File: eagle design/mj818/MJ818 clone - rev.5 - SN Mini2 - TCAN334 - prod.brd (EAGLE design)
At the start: 36 x 36 mm, 39 parts, among them IC202 LDK320AM33R, IC402 STM32F042G6U6, IC501 TCAN334, IC606 MAX16820, IC607 SQA470EEJ-T1_GE3, IC701 MAX16839

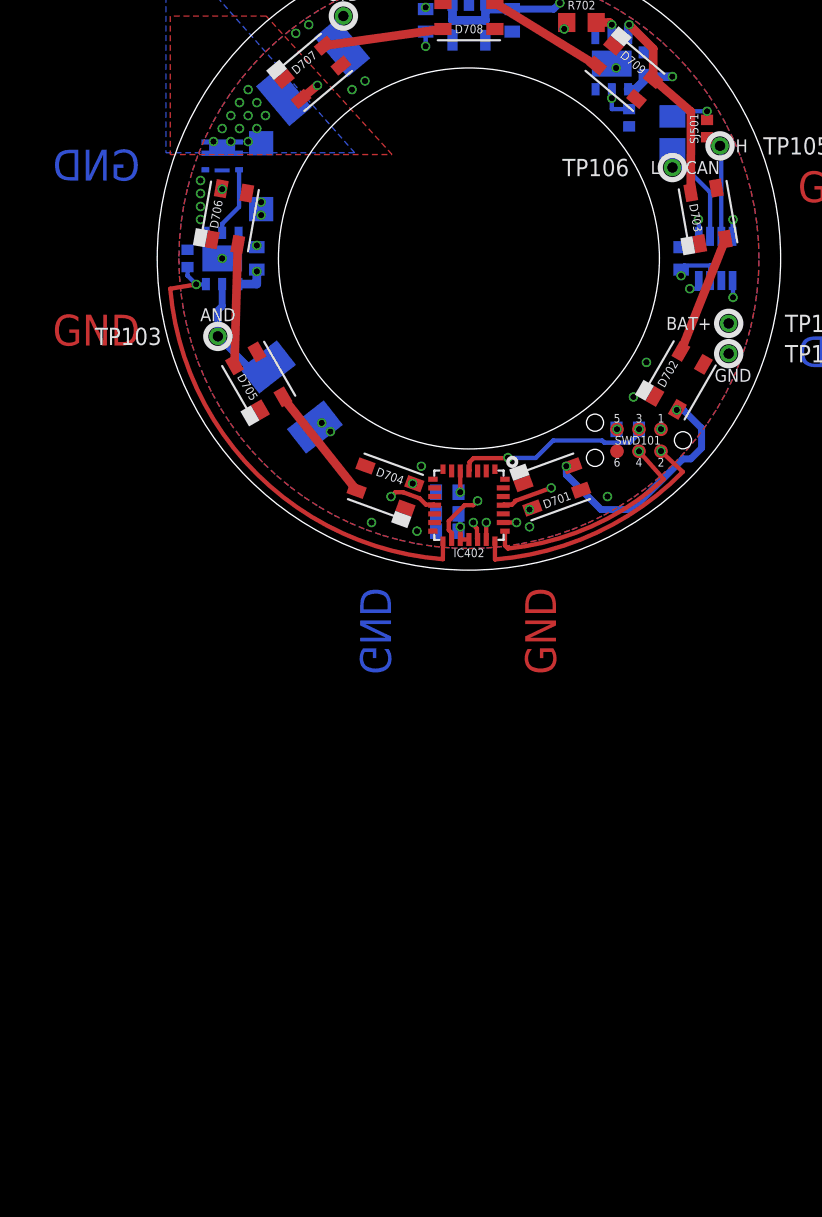
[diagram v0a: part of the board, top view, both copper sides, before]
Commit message: - renamed prod brd & sch files to reflect development for the SuperNova Mini2 housing - added docu & info to reflect housing design
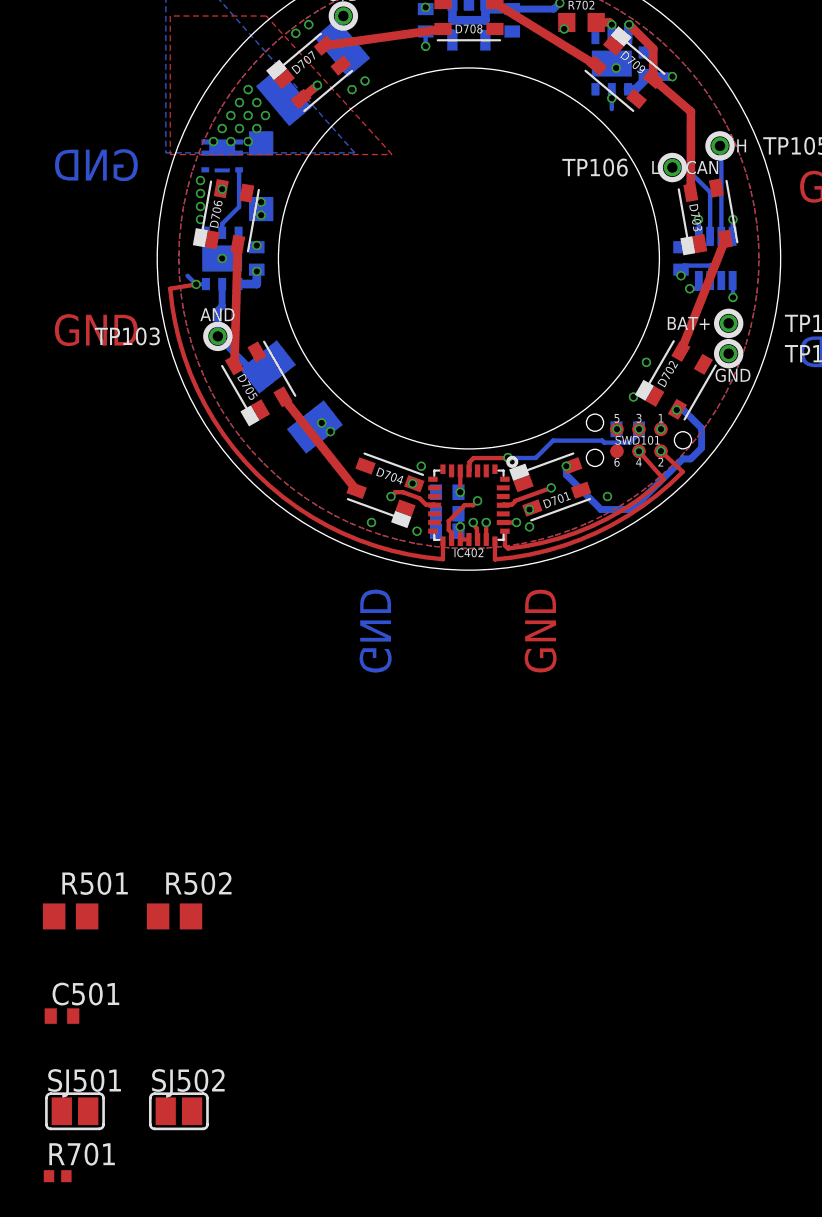
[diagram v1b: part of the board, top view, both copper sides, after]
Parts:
- removed R101, R102: 10k, rcl:R0402
- removed R505: 120, rcl:R0805
- added C501: 47nF / 10V, rcl:C0402
- added R501, R502: 60, rcl:R0805
- added R701: 10k, rcl:R0402
- added SJ502: CAN L term., jumper:SJ
- SJ501: value CAN termination -> CAN H term.; device rcl:R0402 -> jumper:SJ
- moved SJ501 67.5 mm to (-22.8, -49.2), turned to 0 degrees
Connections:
- removed net CAN_INFRA:CAN_JMPR: R505.2, SJ501.1
- new net CAN_INFRA:H: R502.2, SJ501.2
- new net CAN_INFRA:L: R501.1, SJ502.2
- new net CAN_INFRA:SPLIT: C501.1, R501.2, R502.1
- net CAN_H: now also SJ501.1; no longer SJ501.2
- net CAN_L: now also SJ502.1; no longer R505.1
- net DIM_BRAKE: no longer R101.2
- net DIM_REAR: now also R701.2; no longer R102.2
- net GND: now also C501.2, R701.1; no longer R101.1, R102.1
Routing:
- net CAN_INFRA:CAN_JMPR: track 2.62 -> 0.00 mm, vias 1 -> 0
- net CAN_L: track 6.37 -> 5.32 mm
- net DIM_REAR: track 33.0 -> 32.0 mm
- net CAN_H: track 6.21 -> 5.51 mm
- net DIM_BRAKE: track 26.5 -> 26.0 mm
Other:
- board text added: "SuperNova Mini2 housing"

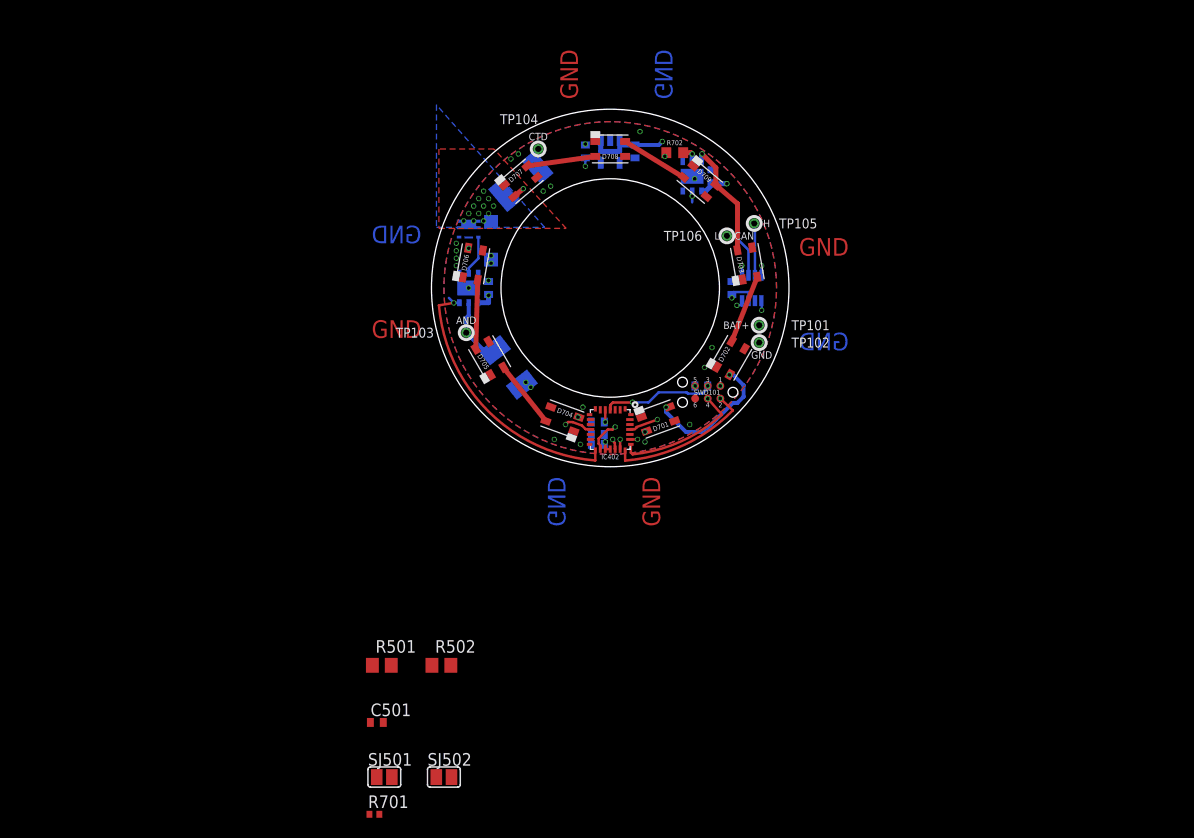
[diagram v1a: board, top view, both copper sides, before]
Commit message: - adjusted PCB outline to match new housing
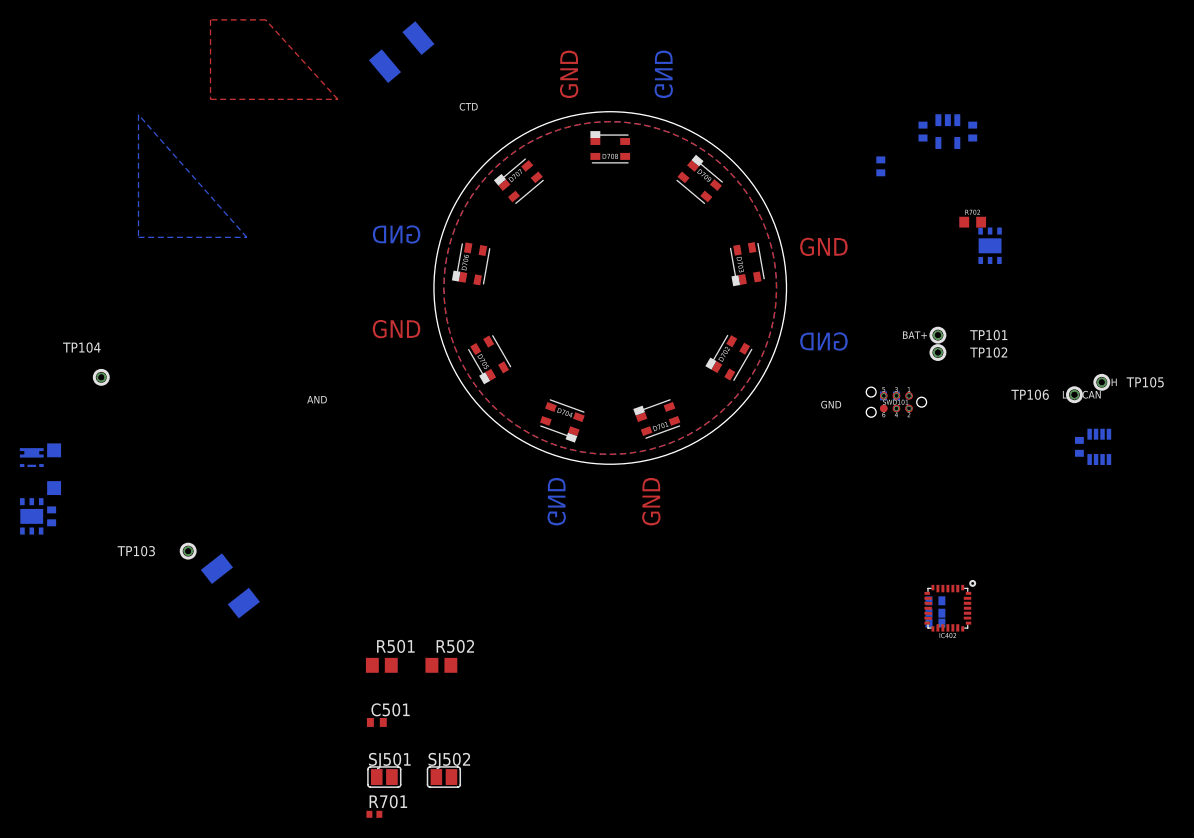
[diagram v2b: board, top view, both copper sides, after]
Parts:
- moved C606 49.6 mm to (-56.2, -23.0)
- moved D601 49.6 mm to (-56.0, -18.2)
- moved IC606 49.6 mm to (-58.2, -23.0)
- moved IC607 49.6 mm to (-58.2, -17.0)
- moved TP104 49.6 mm to (-51.2, -9.00)
- moved C505 38.5 mm to (47.2, -16.0)
- moved IC501 38.5 mm to (49.2, -16.0)
- moved TP105 38.5 mm to (49.5, -9.50)
- moved TP106 38.5 mm to (46.8, -10.8)
- moved C401 38.5 mm to (32.8, -33.8)
- moved C404 38.5 mm to (32.8, -31.5)
- moved C405 38.5 mm to (32.8, -32.8)
- moved IC402 38.5 mm to (34.0, -32.2)
- moved R608 35.6 mm to (-38.2, -30.0)
- moved TP103 35.6 mm to (-42.5, -26.5)
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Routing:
- net BAT+: track 96.5 -> 0.00 mm, vias 10 -> 0
- net REAR_LED_DRIVER:SINK: track 43.1 -> 0.00 mm, vias 2 -> 0
- net !STBY!: track 37.8 -> 0.00 mm, vias 2 -> 0
- net DIM_REAR: track 32.0 -> 0.00 mm, vias 3 -> 0
- net CAN_RX: track 28.7 -> 0.00 mm, vias 2 -> 0
- net CAN_TX: track 28.0 -> 0.00 mm, vias 2 -> 0
- net !SHDN!: track 26.4 -> 0.00 mm, vias 2 -> 0
- net DIM_BRAKE: track 26.0 -> 0.00 mm, vias 1 -> 0
- net SYS_SWDIO: track 14.8 -> 0.00 mm
- net REAR_LED_DRIVER:D1,D2: track 14.1 -> 0.00 mm, vias 2 -> 0
- net SYS_SWCLK: track 13.1 -> 0.00 mm
- net SYS_NRST: track 11.4 -> 0.00 mm, vias 2 -> 1
- net 3V3: track 9.60 -> 0.00 mm, vias 5 -> 1
- net REAR_LED_DRIVER:D2,D3: track 6.97 -> 0.00 mm
- net REAR_LED_DRIVER:D5,D6: track 6.97 -> 0.00 mm
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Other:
- board size 36 x 36 mm -> 35.5 x 35.5 mm

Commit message: - rough routing complete - corrected STM32 pin assignment of prod to match POC - ERC & DRC check out
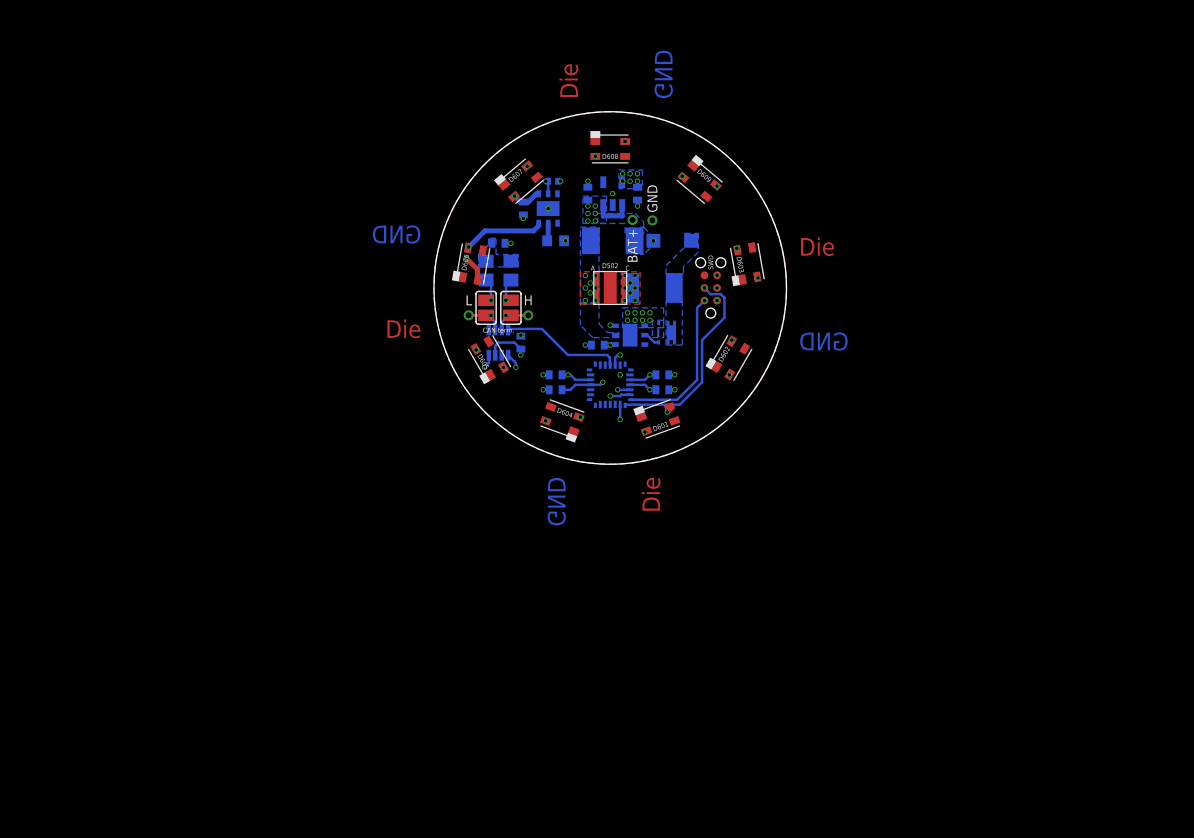
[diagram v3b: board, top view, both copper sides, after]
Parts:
- removed C404: 1u, rcl:C0402
- removed C407: 0.1u, rcl:C0402
- removed C501: 47nF / 10V, rcl:C0402
- removed C505: 0.1μF, rcl:C0402
- removed C606: 1μF / 10V, rcl:C0402
- removed C701: 1μF, rcl:C0402
- removed D701: CLM2D-RCC-CZ0B0BB3, 1374-CLM2D-RCC-ACC-1064252 - Red SMD LED:SMD
- removed IC402: STM32F042G6U6, STM32F042G6:UFQFPN-28
- removed IC501: TCAN334, TCAN33x - 3.3V CAN Transciever:SOT23-8
- removed IC606: MAX16820, MAX16820 LED Driver, constant current:TDFN-6-EP
- removed IC607: SQA470EEJ-T1_GE3, SIA456DJ-T1-GE3 N-Fet:SC-70-6
- removed IC701: MAX16839, MAX16839 LED Driver, constant current:TDFN-6-EP
- removed L601: SDE0604A-270M - 27uH, DE0604A-778075 - Inductor:SMT
- removed R501, R502: 60, rcl:R0805
- removed R608: WSLT2010R2200FEB18 / 0.22Ohm 1W, rcl:R2010
- removed R701: 10k, rcl:R0402
- removed R702: 10R/0.5W, rcl:R0603
- removed SJ501: CAN H term., jumper:SJ
- removed SJ502: CAN L term., jumper:SJ
- removed SWD101: TC2030-NL, tag-connect:TC2030-NL
- removed TP103: LED anode, signal testpoint:TH
- removed TP104: LED cathode, signal testpoint:TH
- added C301, C305, C307: 0.1uF / 10V, rcl:C0402
- added C304: 1uF / 10V, rcl:C0402
- added C506: 1μF / 10V, rcl:C0402
- added C601: 1μF, rcl:C0402
- added D501: PMEG2010ER,115, diode:SOD123
- added D502: Cree XPERED-L1-R250-00401, XLampXPE-221789:SMD
- added IC302: STM32F042G6U6, STM32F042G6:UFQFPN-28
- added IC401: TCAN334, TCAN33x - 3.3V CAN Transciever:SOT23-8
- added IC506: MAX16820, MAX16820 LED Driver, constant current:TDFN-6-EP
- added IC507: SQA470EEJ-T1_GE3, SIA456DJ-T1-GE3 N-Fet:SC-70-6
- added IC601: MAX16839, MAX16839 LED Driver, constant current:TDFN-6-EP
- added L501: SDE0604A-270M - 27uH, DE0604A-778075 - Inductor:SMT
- added R401, R402: 60, rcl:R0805
- added R508: WSLT2010R2200FEB18 / 0.22Ohm 1W, rcl:R2010
- added R601: 10k, rcl:R0402
- added R602: 10R/0.5W, rcl:R0603
- added SJ401: CAN H term., jumper:SJ
- added SJ402: CAN L term., jumper:SJ
- added SWD1: TC2030-NL, tag-connect:TC2030-NL
- C207: value 1μF -> 1uF / 10V
- C401: value 0.1u -> 47nF / 10V
- C405: value 0.1u -> 0.1uF / 10V
- D601: value PMEG2010ER,115 -> CLM2D-RCC-CZ0B0BB3; device diode:SOD123 -> 1374-CLM2D-RCC-ACC-1064252 - Red SMD LED:SMD
- TP101, TP102, TP105, TP106: device signal testpoint:TH -> signal testpoint:TH-0.6
- moved TP106 61.5 mm to (-14.2, -2.75), flipped to the bottom, turned to 180 degrees
- moved D601 61.0 mm to (4.82, -13.2), flipped to the top, turned to 20 degrees
- moved C401 58.3 mm to (-11.2, 4.50)
- moved TP105 58.1 mm to (-8.25, -2.75), flipped to the bottom
- moved C405 49.9 mm to (-9.00, -5.50), turned to 90 degrees
- moved C202 39.3 mm to (-2.25, 9.50), turned to 90 degrees
- moved IC202 34.3 mm to (0.25, 9.50), turned to 180 degrees
- moved TP101 32.9 mm to (2.25, 6.85), flipped to the bottom
- moved TP102 31.7 mm to (4.25, 6.80), flipped to the bottom
- moved C207 29.4 mm to (2.75, 9.50), turned to 90 degrees
- renumbered D702 to D602, D703 to D603, D704 to D604, D705 to D605, D706 to D606, D707 to D607, D708 to D608, D709 to D609
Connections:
- removed net !SHDN!: IC402.25_PB4, IC501.P$5
- removed net LED_AN: IC606.CSN, R608.1, TP103.TP$1
- removed net LED_CA: L601.P$1, TP104.TP$1
- new net BRAKE_LED_DRIVER:DIE: D502.DIE
- new net BRAKE_LED_DRIVER:LED_AN: D502.AND, IC506.CSN, R508.1
- new net BRAKE_LED_DRIVER:LED_CA: D502.CAT, L501.P$1
- net !STBY!: now also IC302.11_PA5, IC401.P$8; no longer IC402.11_PA5, IC501.P$8
- net 3V3: now also C301.2, C304.2, C305.2, C405.1, IC302.17_VDD, IC302.18_VDDIO2, IC302.5_VDDA, IC401.P$3, SWD1.1_TVCC; no longer C401.2, C404.2, C405.2, C505.1, IC402.17_VDD, IC402.18_VDDIO2, IC402.5_VDDA, IC501.P$3, SWD101.1_TVCC
- net BAT+: now also C506.1, C601.2, D501.C, D601.2, IC506.IN, IC601.IN, R508.2; no longer C606.1, C701.2, D601.C, D701.2, IC606.IN, IC701.IN, R608.2
- net BRAKE_LED_DRIVER:DIM_BRAKE_DRAIN: now also D501.A, IC507.1D, IC507.2D, IC507.5D, IC507.6D, IC507.D, L501.P$2; no longer D601.A, IC607.1D, IC607.2D, IC607.5D, IC607.6D, IC607.D, L601.P$2
- net BRAKE_LED_DRIVER:DIM_BRAKE_GATE: now also IC506.DRV, IC507.3G; no longer IC606.DRV, IC607.3G
- net BRAKE_LED_DRIVER:VCC: now also IC506.VCC; no longer IC606.VCC
- net CAN_H: now also IC401.P$7, SJ401.1; no longer IC501.P$7, SJ501.1
- net CAN_INFRA:H: now also R402.2, SJ401.2; no longer R502.2, SJ501.2
- net CAN_INFRA:L: now also R401.1, SJ402.2; no longer R501.1, SJ502.2
- net CAN_INFRA:SPLIT: now also C401.1, R401.2, R402.1; no longer C501.1, R501.2, R502.1
- net CAN_L: now also IC401.P$6, SJ402.1; no longer IC501.P$6, SJ502.1
- net CAN_RX: now also IC302.19_PA9-[PA11], IC401.P$4; no longer IC402.19_PA9-[PA11], IC501.P$4
- net CAN_TX: now also IC302.20_PA10-[PA12], IC401.P$1; no longer IC402.20_PA10-[PA12], IC501.P$1
- net DIM_BRAKE: now also IC302.12_PA6, IC506.DIM; no longer IC402.15_PB1, IC606.DIM
- net DIM_REAR: now also IC302.23_PA15, IC601.DIM, R601.2; no longer IC402.23_PA15, IC701.DIM, R701.2
- net GND: now also C301.1, C304.1, C305.1, C307.1, C401.2, C405.2, C506.2, C601.1, IC302.16_VSS, IC401.P$2, IC506.GND, IC506.GND1, IC507.4S, IC507.S, IC601.FLTS, IC601.GND, IC601.GND1, R601.1, R602.2, SWD1.5_GND; no longer C401.1, C404.1, C405.1, C407.1, C501.2, C505.2, C606.2, C701.1, IC402.16_VSS, IC501.P$2, IC606.GND, IC606.GND1, IC607.4S, IC607.S, IC701.FLTS, IC701.GND, IC701.GND1, R701.1, R702.2, SWD101.5_GND
- net REAR_LED_DRIVER:CS: now also IC601.CS, R602.1; no longer IC701.CS, R702.1
- net REAR_LED_DRIVER:D1,D2: now also D601.4; no longer D701.4
- net REAR_LED_DRIVER:SINK: now also IC601.SINK; no longer IC701.SINK
- net SYS_NRST: now also C307.2, IC302.4_NRST, SWD1.3_T_NRST; no longer C407.2, IC402.4_NRST, SWD101.3_T_NRST
- net SYS_SWCLK: now also IC302.22_PA14, SWD1.4_T_SWCLK; no longer IC402.22_PA14, SWD101.4_T_SWCLK
- net SYS_SWDIO: now also IC302.21_PA13, SWD1.2_T_SWDIO; no longer IC402.21_PA13, SWD101.2_T_SWDIO
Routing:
- net BAT+: track 0.00 -> 46.7 mm, vias 0 -> 11
- net REAR_LED_DRIVER:SINK: track 0.00 -> 43.9 mm, vias 0 -> 3
- net DIM_REAR: track 0.00 -> 30.8 mm, vias 0 -> 2
- net SYS_NRST: track 0.00 -> 21.2 mm, vias 1 -> 2
- net SYS_SWCLK: track 0.00 -> 20.6 mm
- net CAN_RX: track 0.00 -> 19.0 mm, vias 0 -> 2
- net SYS_SWDIO: track 0.00 -> 15.8 mm
- net CAN_TX: track 0.00 -> 14.5 mm, vias 0 -> 2
- net 3V3: track 0.00 -> 13.3 mm, vias 1 -> 11
- net REAR_LED_DRIVER:D5,D6: track 0.00 -> 12.6 mm, vias 0 -> 2
- net !STBY!: track 0.00 -> 12.3 mm
- net REAR_LED_DRIVER:D1,D2: track 0.00 -> 8.08 mm, vias 0 -> 2
- net REAR_LED_DRIVER:D2,D3: track 0.00 -> 7.04 mm, vias 0 -> 2
- net REAR_LED_DRIVER:D7,D8: track 0.00 -> 6.99 mm, vias 0 -> 2
- net REAR_LED_DRIVER:D8,D9: track 0.00 -> 6.91 mm, vias 0 -> 2
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- added copper zone on layer 16, net 3V3
- added copper zone on layer 16, net BAT+
- added copper zone on layer 2, net BAT+
- added copper zone on layer 1, net BRAKE_LED_DRIVER:DIE
- added copper zone on layer 1, net BRAKE_LED_DRIVER:LED_AN
- added copper zone on layer 16, net BRAKE_LED_DRIVER:LED_AN
- added copper zone on layer 1, net BRAKE_LED_DRIVER:LED_CA
- added copper zone on layer 16, net CAN_INFRA:SPLIT
- removed copper zone on layer 1, net BRAKE_LED_DRIVER:DIM_BRAKE_DRAIN
- removed copper zone on layer 1, net GND
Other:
- board text added: "CAN term."
- board text added: "Die"
- board text added: "SuperNova Mini2 clone ejovrh rev. 5a"
- board text removed: "AND"
- board text removed: "CAN"
- board text removed: "CTD"
- board text removed: "MJ818 clone"
- board text removed: "ejovrh rev.5"

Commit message: - changed size of shunt for rear light to 1206 - finished routing - created BOM - ERC & DRC check out ok
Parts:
- C202, C506: value 1μF / 10V -> 1uF / 10V
- C601: value 1μF -> 1uF / 10V
- R401, R402: value 60 -> 60R, 0.5W
- R602: device rcl:R0603 -> rcl:R1206
- moved R602 3.09 mm to (-6.25, 1.75), turned to 270 degrees
- moved TP102 1.06 mm to (5.00, 7.55)
- moved C202 0.75 mm to (-2.25, 10.2)
- moved C207 0.75 mm to (2.75, 10.2)
- moved IC202 0.75 mm to (0.25, 10.2)
- moved TP101 0.65 mm to (2.25, 7.50)
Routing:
- net SYS_SWDIO: track 15.8 -> 13.6 mm, vias 1 -> 2
- net REAR_LED_DRIVER:CS: track 1.81 -> 3.35 mm
- net SYS_NRST: track 21.2 -> 20.5 mm
- net CAN_RX: track 19.0 -> 19.6 mm
- net BAT+: track 46.7 -> 46.0 mm
- net SYS_SWCLK: track 20.6 -> 20.0 mm, vias 1 -> 2
- net GND: vias 24 -> 26
- added copper zone on layer 1, net CUT
- added copper zone on layer 16, net CUT
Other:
- board text added: "Mj818 clone SuperNova Mini2 ejovrh rev. 5a"
- board text removed: "SuperNova Mini2 clone ejovrh rev. 5a"
